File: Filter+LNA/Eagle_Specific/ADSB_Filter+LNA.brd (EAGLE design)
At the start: 105.3 x 45.7 mm, 12 parts, among them U1 BFP420, X1 SMA-142-0701-801/806, X2 SMA-142-0701-801/806

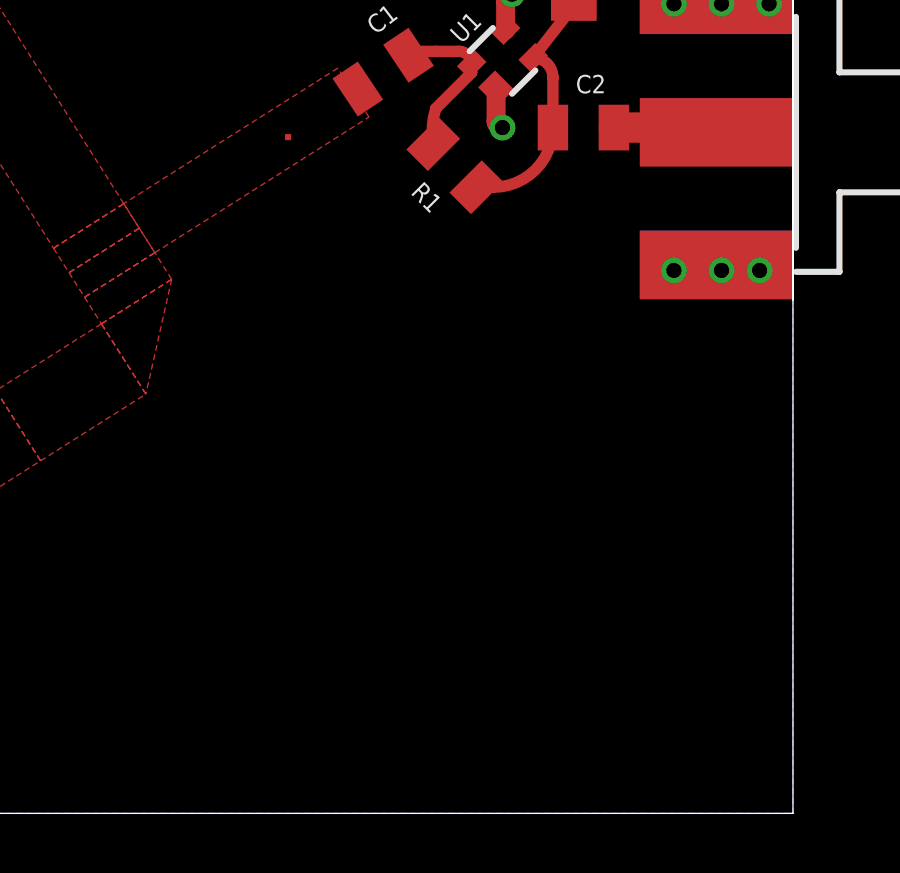
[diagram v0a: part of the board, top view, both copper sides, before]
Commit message: Minor changes to Filter+LNA Layout
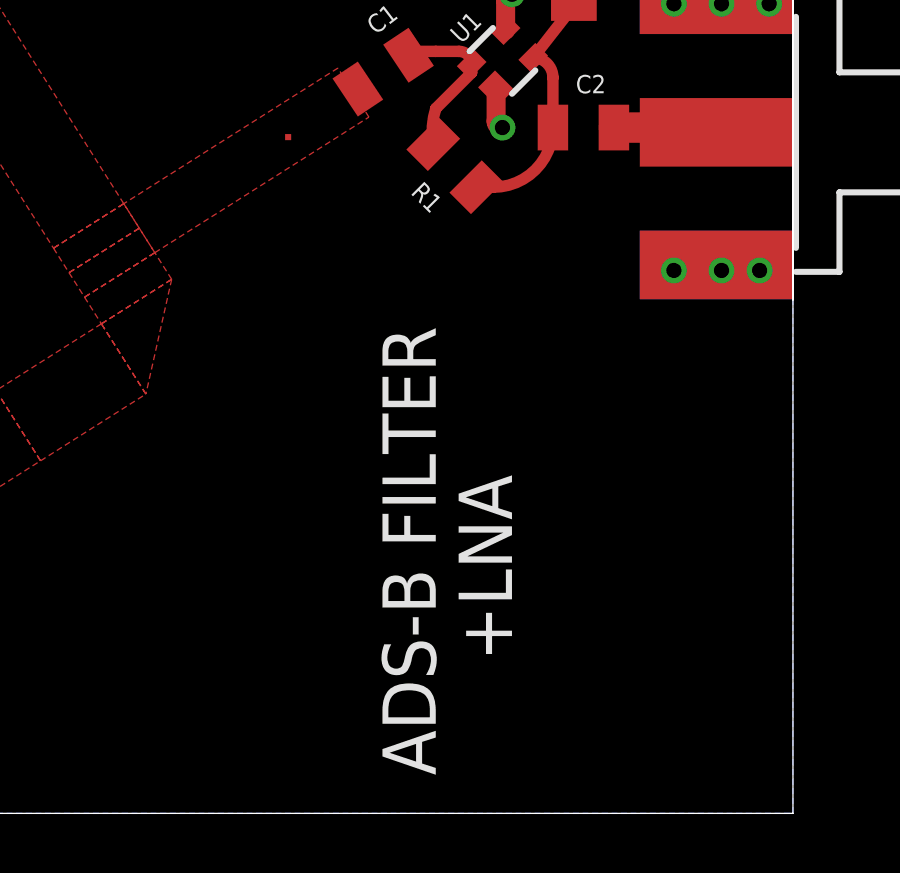
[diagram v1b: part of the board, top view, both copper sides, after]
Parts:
- removed U$1: RTLSDR-LARGE, logos:RTLSDR-LARGE
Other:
- board text added: "+LNA"
- board text added: "ADS-B FILTER"
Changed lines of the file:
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@@
 <wire x1="19.52625" y1="25.3875" x2="-85.725" y2="25.3875" width="0" layer="20"/>
 <wire x1="-85.725" y1="25.3875" x2="-85.725" y2="-20.32" width="0" layer="20"/>
-<polygon width="0.0254" layer="29">
+<polygon width="0.1524" layer="29">
 <vertex x="5.08" y="2.54"/>
 <vertex x="5.08" y="21.59"/>
@@
 <vertex x="-80.01" y="-16.51"/>
 <vertex x="-77.47" y="-19.05"/>
-<vertex x="2.2225" y="-19.05"/>
+<vertex x="2.54" y="-19.05"/>
 <vertex x="5.08" y="-16.51"/>
 <vertex x="5.08" y="5.08"/>
 </polygon>
-<polygon width="0.0254" layer="30">
+<polygon width="0.1524" layer="30">
 <vertex x="-77.47" y="24.13"/>
 <vertex x="-80.01" y="21.59"/>
 <vertex x="-80.01" y="-16.51"/>
 <vertex x="-77.47" y="-19.05"/>
-<vertex x="2.2225" y="-19.05"/>
+<vertex x="2.54" y="-19.05"/>
 <vertex x="5.08" y="-16.51"/>
 <vertex x="5.08" y="21.59"/>
@@
 <text x="7.62" y="11.1125" size="1.778" layer="25" rot="R90">CC-BY-SA</text>
 <text x="10.16" y="11.1125" size="1.778" layer="25" rot="R90">by NØRC</text>
+<text x="7.62" y="-19.05" size="1.778" layer="25" ratio="19" rot="R90">ADS-B FILTER</text>
+<text x="10.16" y="-15.24" size="1.778" layer="25" ratio="19" rot="R90">+LNA</text>
 </plain>
 <attributes>
@@
 <element name="TP3" library="Pads_Test_Points" package="SMD_8_8" value="TEST_POINTS8_8" x="-79.21625" y="2.69875" smashed="yes"/>
 <element name="TP4" library="Pads_Test_Points" package="SMD_8_8" value="TEST_POINTS8_8" x="2.69875" y="2.2225" smashed="yes"/>
-<element name="U$1" library="logos" package="RTLSDR-LARGE" value="RTLSDR-LARGE" x="3.175" y="3.4925" rot="MR180"/>
 </elements>
 <signals>
